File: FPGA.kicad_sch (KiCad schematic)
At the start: 1 part

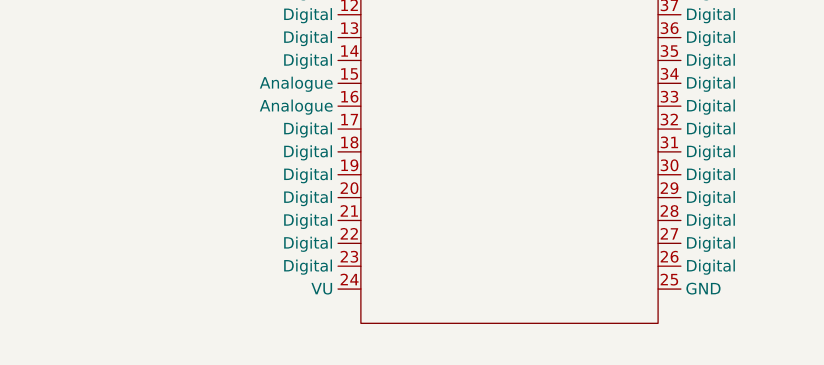
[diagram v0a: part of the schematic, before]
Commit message: Added power supply and standardised on pwer supply net names
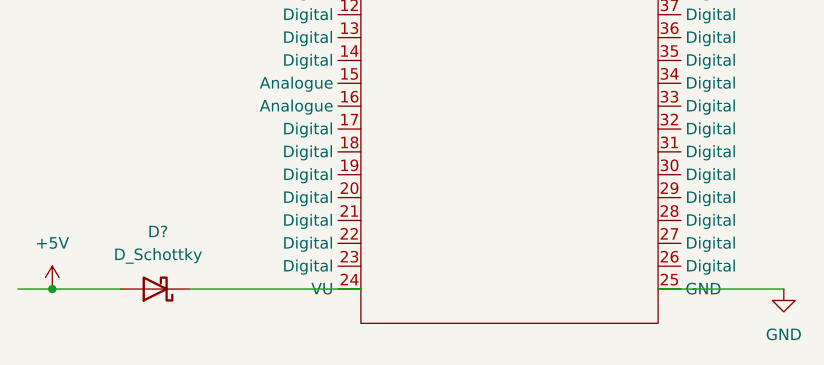
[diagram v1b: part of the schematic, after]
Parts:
- added D?: D_Schottky, symbol Device:D_Schottky
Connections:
- net at FPGA?.24 (VU): now also D?.1 (K)
- net GND: now reaches FPGA?.25 (GND)
- new net +5V: D?.2 (A)
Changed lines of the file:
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@@
 (kicad_sch (version 20211123) (generator eeschema)
   (paper "A4")
+  (junction (at 90.17 118.11) (diameter 0) (color 0 0 0 0)
+  )
+  (wire (pts (xy 90.17 118.11) (xy 97.79 118.11))
+    (stroke (width 0) (type default) (color 0 0 0 0))
+  )
+  (wire (pts (xy 105.41 118.11) (xy 124.46 118.11))
+    (stroke (width 0) (type default) (color 0 0 0 0))
+  )
+  (wire (pts (xy 86.36 118.11) (xy 90.17 118.11))
+    (stroke (width 0) (type default) (color 0 0 0 0))
+  )
+  (wire (pts (xy 157.48 118.11) (xy 171.45 118.11))
+    (stroke (width 0) (type default) (color 0 0 0 0))
+  )
+  (symbol (lib_id "power:GND") (at 171.45 118.11 0) (unit 1)
+    (in_bom yes) (on_board yes) (fields_autoplaced)
+    (property "Reference" "#PWR?" (id 0) (at 171.45 124.46 0)
+      (effects (font (size 1.27 1.27)) hide)
+    )
+    (property "Value" "GND" (id 1) (at 171.45 123.19 0))
+    (property "Footprint" "" (id 2) (at 171.45 118.11 0)
+      (effects (font (size 1.27 1.27)) hide)
+    )
+    (property "Datasheet" "" (id 3) (at 171.45 118.11 0)
+      (effects (font (size 1.27 1.27)) hide)
+    )
+    (pin "1")
+  )
+  (symbol (lib_id "Device:D_Schottky") (at 101.6 118.11 180) (unit 1)
+    (in_bom yes) (on_board yes) (fields_autoplaced)
+    (property "Reference" "D?" (id 0) (at 101.9175 111.76 0))
+    (property "Value" "D_Schottky" (id 1) (at 101.9175 114.3 0))
+    (property "Footprint" "" (id 2) (at 101.6 118.11 0)
+      (effects (font (size 1.27 1.27)) hide)
+    )
+    (property "Datasheet" "~" (id 3) (at 101.6 118.11 0)
+      (effects (font (size 1.27 1.27)) hide)
+    )
+    (pin "1")
+    (pin "2")
+  )
   (symbol (lib_id "local_library:FPGA") (at 140.97 104.14 0) (unit 1)
     (in_bom yes) (on_board yes) (fields_autoplaced)
@@
     (pin "9")
   )
+  (symbol (lib_id "power:+5V") (at 90.17 118.11 0) (unit 1)
+    (in_bom yes) (on_board yes) (fields_autoplaced)
+    (property "Reference" "#PWR?" (id 0) (at 90.17 121.92 0)
+      (effects (font (size 1.27 1.27)) hide)
+    )
+    (property "Value" "+5V" (id 1) (at 90.17 113.03 0))
+    (property "Footprint" "" (id 2) (at 90.17 118.11 0)
+      (effects (font (size 1.27 1.27)) hide)
+    )
+    (property "Datasheet" "" (id 3) (at 90.17 118.11 0)
+      (effects (font (size 1.27 1.27)) hide)
+    )
+    (pin "1")
+  )
 )

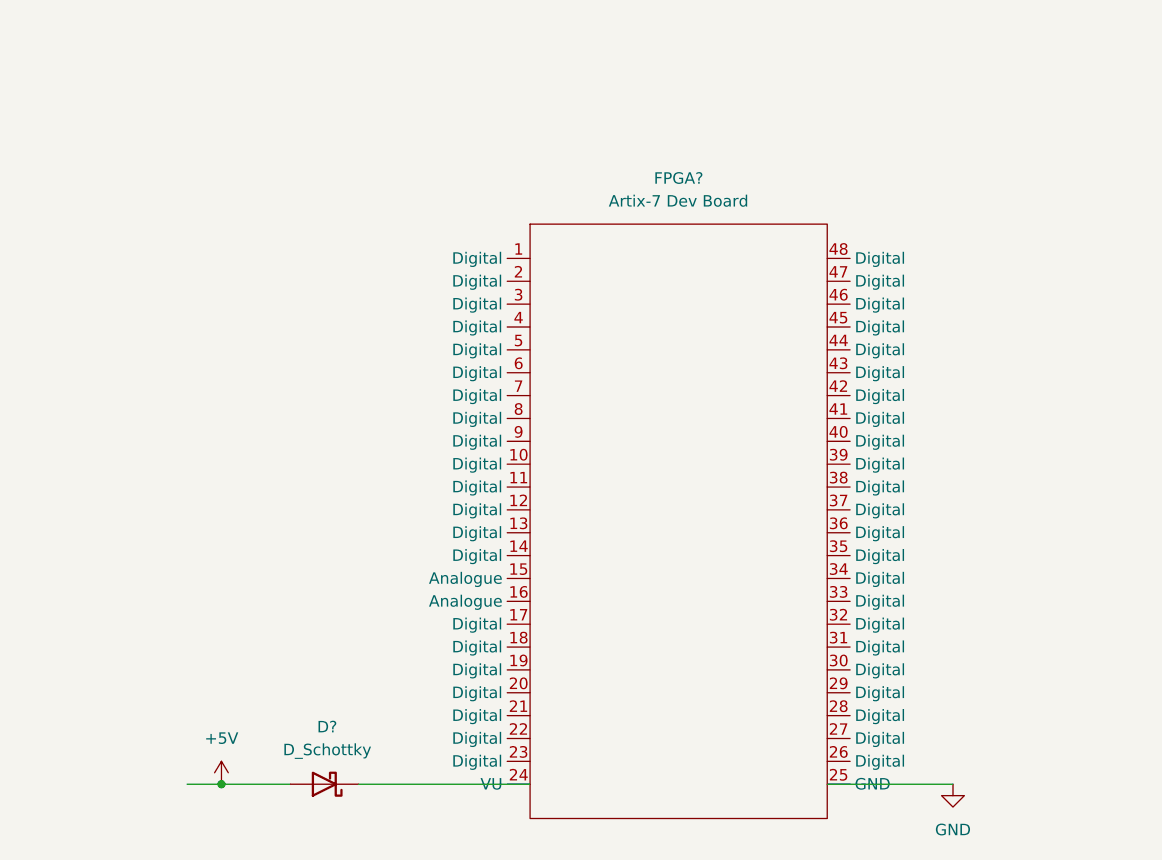
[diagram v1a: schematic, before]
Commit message: add component numbers to schematic
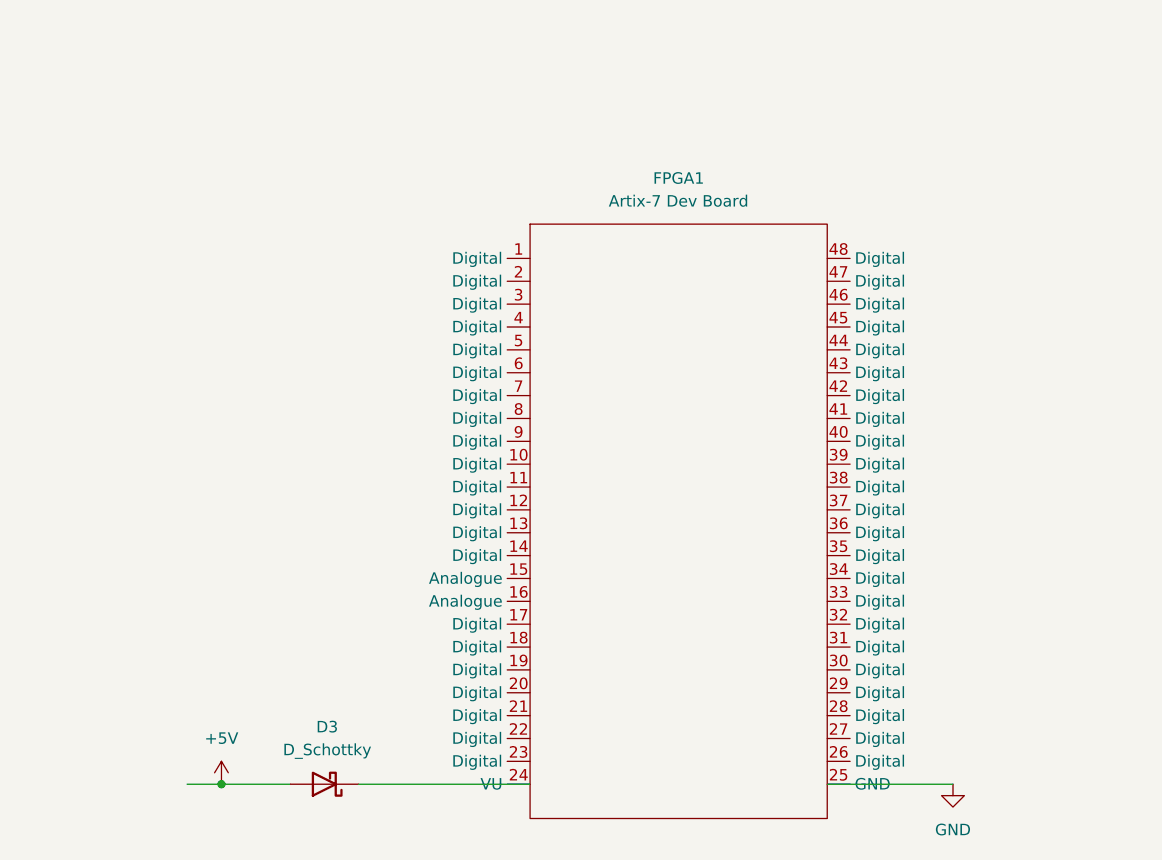
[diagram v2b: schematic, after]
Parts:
- gave numbers to parts that had none: 2
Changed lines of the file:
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@@
   (symbol (lib_id "power:GND") (at 171.45 118.11 0) (unit 1)
     (in_bom yes) (on_board yes) (fields_autoplaced)
-    (property "Reference" "#PWR?" (id 0) (at 171.45 124.46 0)
+    (property "Reference" "#PWR028" (id 0) (at 171.45 124.46 0)
       (effects (font (size 1.27 1.27)) hide)
     )
@@
   (symbol (lib_id "Device:D_Schottky") (at 101.6 118.11 180) (unit 1)
     (in_bom yes) (on_board yes) (fields_autoplaced)
-    (property "Reference" "D?" (id 0) (at 101.9175 111.76 0))
+    (property "Reference" "D3" (id 0) (at 101.9175 111.76 0))
     (property "Value" "D_Schottky" (id 1) (at 101.9175 114.3 0))
     (property "Footprint" "" (id 2) (at 101.6 118.11 0)
@@
   (symbol (lib_id "local_library:FPGA") (at 140.97 104.14 0) (unit 1)
     (in_bom yes) (on_board yes) (fields_autoplaced)
-    (property "Reference" "FPGA?" (id 0) (at 140.97 50.8 0))
+    (property "Reference" "FPGA1" (id 0) (at 140.97 50.8 0))
     (property "Value" "Artix-7 Dev Board" (id 1) (at 140.97 53.34 0))
     (property "Footprint" "" (id 2) (at 140.97 104.14 0)
@@
   (symbol (lib_id "power:+5V") (at 90.17 118.11 0) (unit 1)
     (in_bom yes) (on_board yes) (fields_autoplaced)
-    (property "Reference" "#PWR?" (id 0) (at 90.17 121.92 0)
+    (property "Reference" "#PWR027" (id 0) (at 90.17 121.92 0)
       (effects (font (size 1.27 1.27)) hide)
     )

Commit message: fix nets and wire FPGA
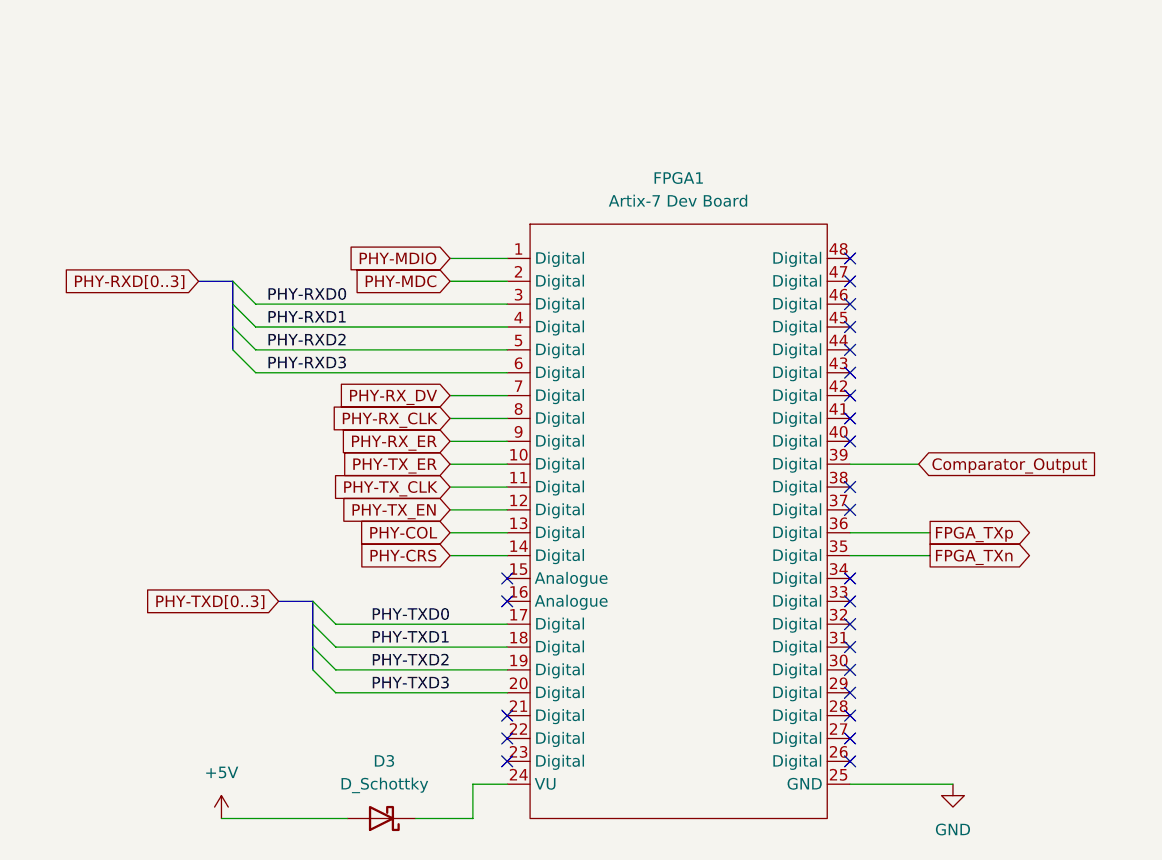
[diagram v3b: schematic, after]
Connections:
- net PHY-MDIO: now reaches FPGA1.1 (Digital)
- net PHY-TX_ER: now reaches FPGA1.10 (Digital)
- net PHY-TX_CLK: now reaches FPGA1.11 (Digital)
- net PHY-TX_EN: now reaches FPGA1.12 (Digital)
- net PHY-COL: now reaches FPGA1.13 (Digital)
- net PHY-CRS: now reaches FPGA1.14 (Digital)
- net PHY-TXD0: now reaches FPGA1.17 (Digital)
- net PHY-TXD1: now reaches FPGA1.18 (Digital)
- net PHY-TXD2: now reaches FPGA1.19 (Digital)
- net PHY-MDC: now reaches FPGA1.2 (Digital)
- net PHY-TXD3: now reaches FPGA1.20 (Digital)
- net PHY-RXD0: now reaches FPGA1.3 (Digital)
- net FPGA_TXn: now reaches FPGA1.35 (Digital)
- net FPGA_TXp: now reaches FPGA1.36 (Digital)
- net Comparator_Output: now reaches FPGA1.39 (Digital)
- net PHY-RXD1: now reaches FPGA1.4 (Digital)
- net PHY-RXD2: now reaches FPGA1.5 (Digital)
- net PHY-RXD3: now reaches FPGA1.6 (Digital)
- net PHY-RX_DV: now reaches FPGA1.7 (Digital)
- net PHY-RX_CLK: now reaches FPGA1.8 (Digital)
- net PHY-RX_ER: now reaches FPGA1.9 (Digital)
- no-connect marks 0 -> 25
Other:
- moved on the sheet: D3, FPGA1

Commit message: Add footprints to SMA connectors and FPGA
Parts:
- FPGA1: footprint (none) -> OUR_FOOTPRINTS:FPGA
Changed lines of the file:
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@@
     (property "Reference" "FPGA1" (id 0) (at 140.97 50.8 0))
     (property "Value" "Artix-7 Dev Board" (id 1) (at 140.97 53.34 0))
-    (property "Footprint" "" (id 2) (at 140.97 104.14 0)
+    (property "Footprint" "OUR_FOOTPRINTS:FPGA" (id 2) (at 140.97 104.14 0)
       (effects (font (size 1.27 1.27)) hide)
     )

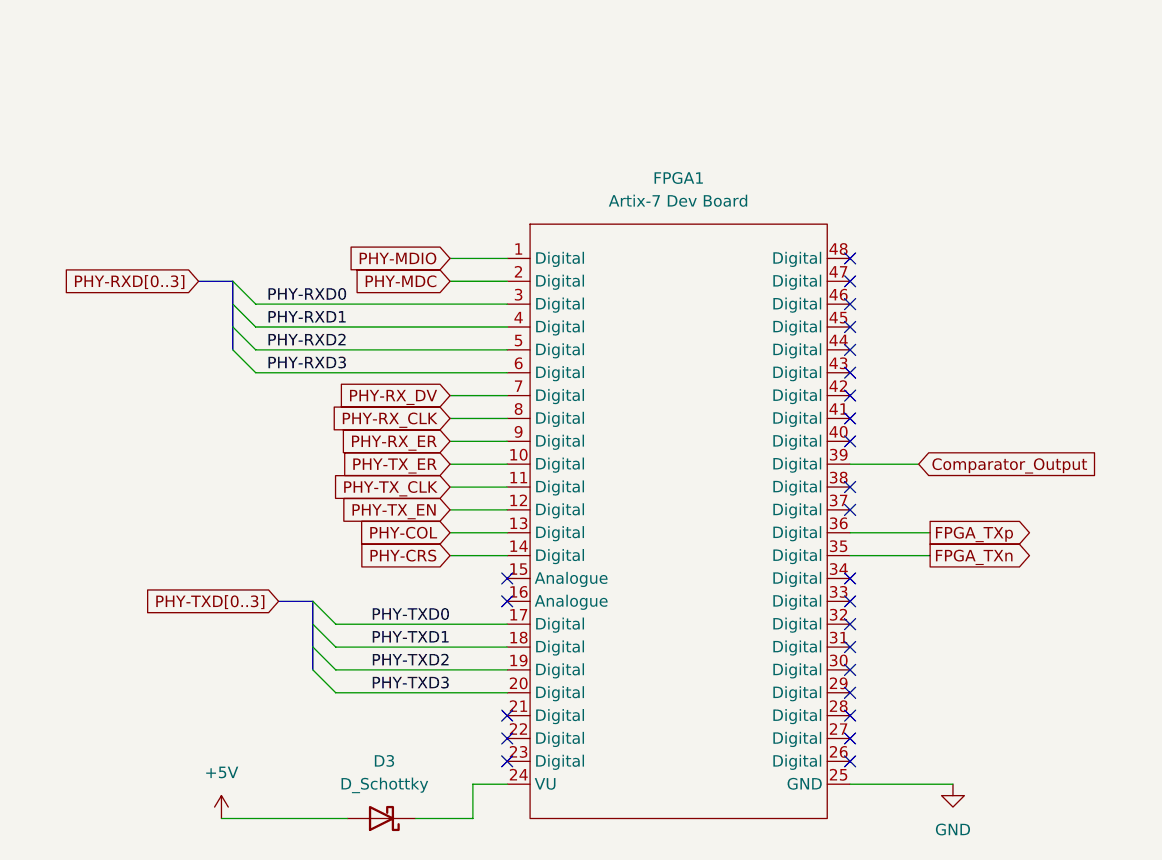
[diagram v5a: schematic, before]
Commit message: Assign footprints to ICs
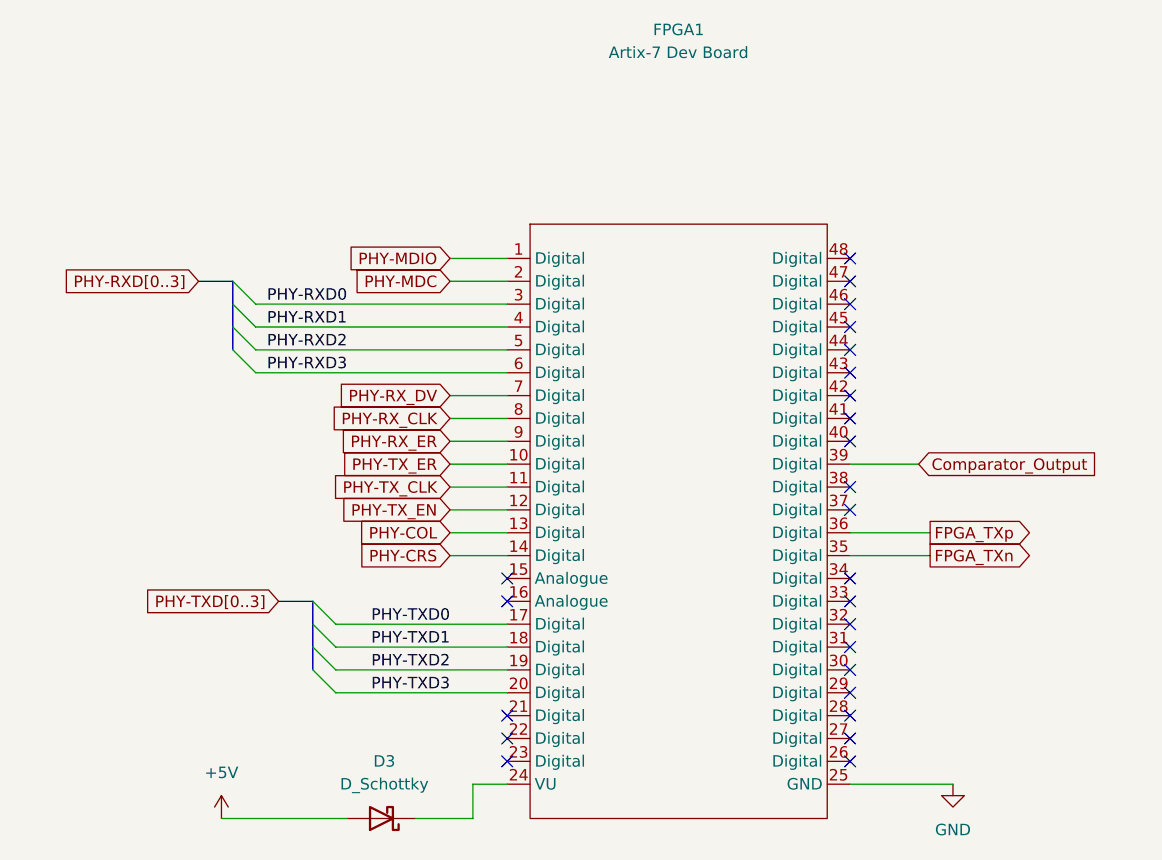
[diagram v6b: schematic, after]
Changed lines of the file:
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@@
     (pin "2")
   )
-  (symbol (lib_id "local_library:FPGA") (at 140.97 104.14 0) (unit 1)
+  (symbol (lib_id "local_library:FPGA") (at 140.97 87.63 0) (unit 1)
     (in_bom yes) (on_board yes) (fields_autoplaced)
-    (property "Reference" "FPGA1" (id 0) (at 140.97 50.8 0))
-    (property "Value" "Artix-7 Dev Board" (id 1) (at 140.97 53.34 0))
-    (property "Footprint" "OUR_FOOTPRINTS:FPGA" (id 2) (at 140.97 104.14 0)
+    (property "Reference" "FPGA1" (id 0) (at 140.97 34.29 0))
+    (property "Value" "Artix-7 Dev Board" (id 1) (at 140.97 36.83 0))
+    (property "Footprint" "OUR_FOOTPRINTS:FPGA" (id 2) (at 140.97 87.63 0)
       (effects (font (size 1.27 1.27)) hide)
     )
-    (property "Datasheet" "" (id 3) (at 140.97 104.14 0)
+    (property "Datasheet" "" (id 3) (at 140.97 87.63 0)
       (effects (font (size 1.27 1.27)) hide)
     )

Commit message: Assign footprints to everything bar inductors
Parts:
- D3: footprint (none) -> Diode_SMD:D_SOD-123F
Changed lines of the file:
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@@
     (property "Reference" "D3" (id 0) (at 108.2675 115.57 0))
     (property "Value" "D_Schottky" (id 1) (at 108.2675 118.11 0))
-    (property "Footprint" "" (id 2) (at 107.95 121.92 0)
+    (property "Footprint" "Diode_SMD:D_SOD-123F" (id 2) (at 107.95 121.92 0)
       (effects (font (size 1.27 1.27)) hide)
     )
